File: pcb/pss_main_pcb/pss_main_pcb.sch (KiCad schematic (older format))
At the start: 3 parts

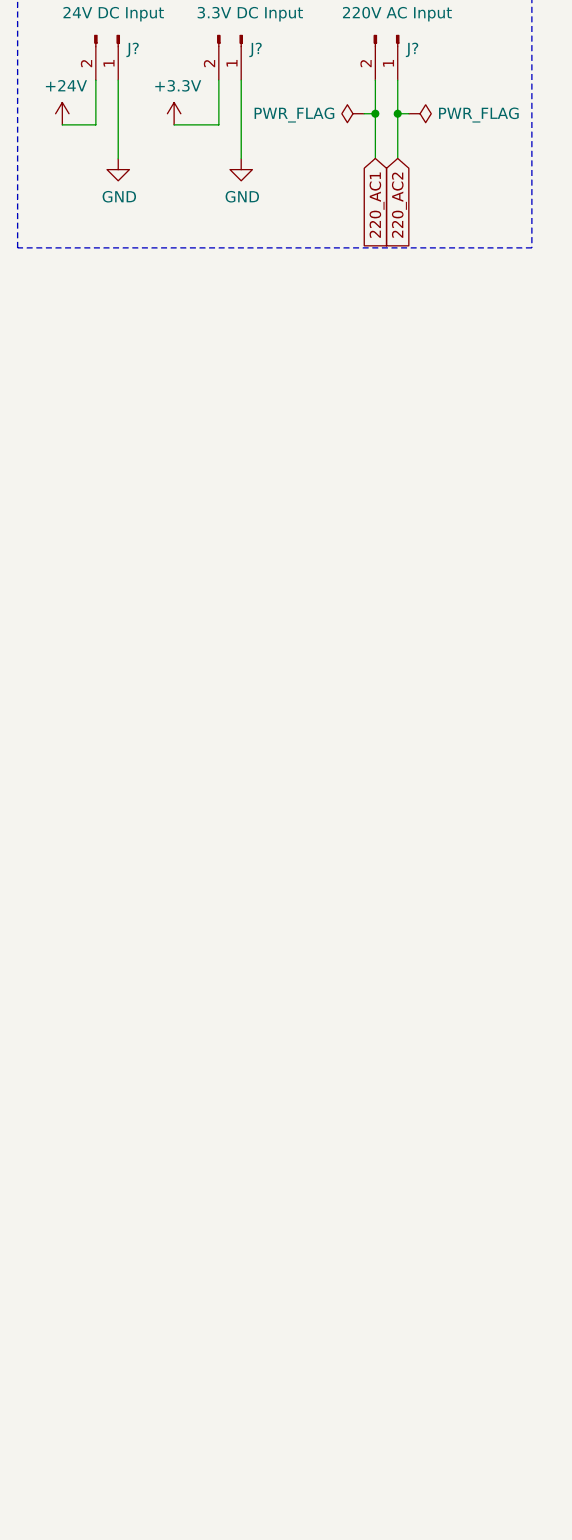
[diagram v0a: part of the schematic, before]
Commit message: Add connectors to schematics
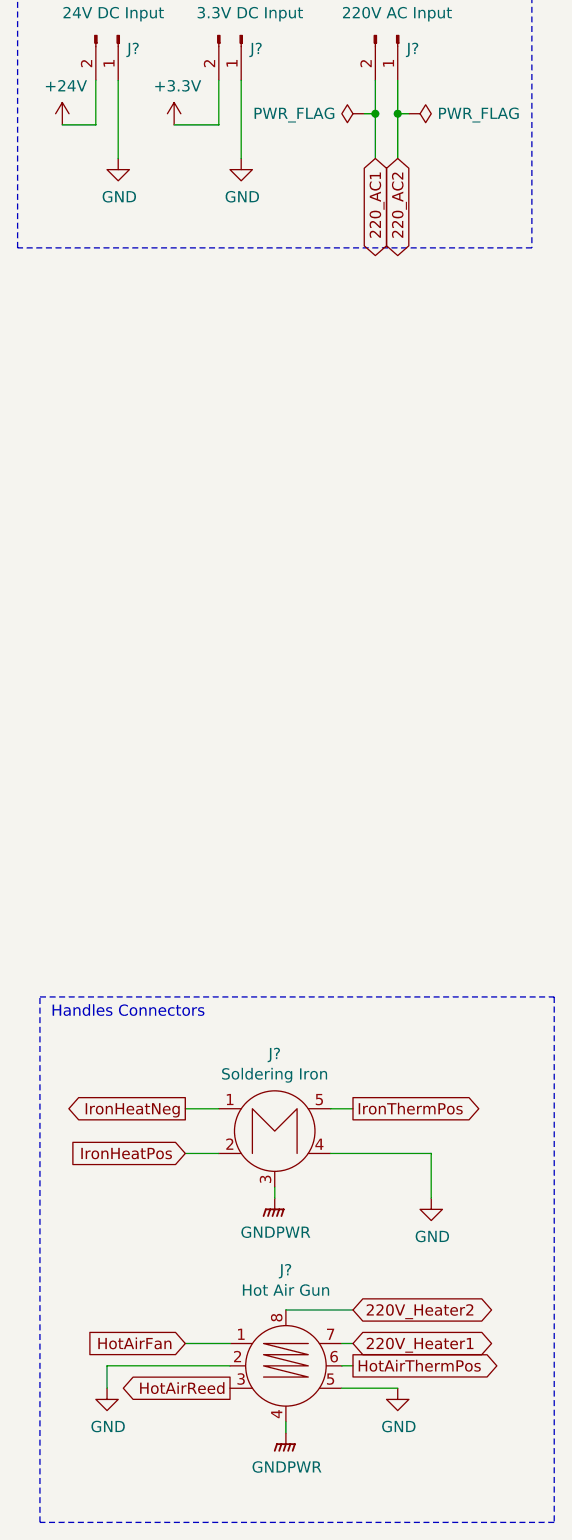
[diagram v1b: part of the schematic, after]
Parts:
- added J?: Soldering Iron, symbol gx16_conn:GX16-M5_connector
- added J?: Hot Air Gun, symbol gx16_conn:GX16-M8_connector
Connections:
- net GND: now also J?.2, J?.4, J?.5
- new net 220V_Heater1: J?.7
- new net 220V_Heater2: J?.8
- new net GNDPWR: J?.3, J?.4
- new net HotAirFan: J?.1
- new net HotAirReed: J?.3
- new net HotAirThermPos: J?.6
- new net IronHeatNeg: J?.1
- new net IronHeatPos: J?.2
- new net IronThermPos: J?.5
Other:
- note added: "Handles Connectors\n"
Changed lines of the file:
@@
 Wire Wire Line
 	2300 1350 2350 1350
-Text GLabel 2200 1550 3    50   Input ~ 0
+Text GLabel 2200 1550 3    50   BiDi ~ 0
 220_AC1
 Wire Wire Line
 	2200 1550 2200 1350
 Connection ~ 2200 1350
-Text GLabel 2300 1550 3    50   Input ~ 0
+Text GLabel 2300 1550 3    50   BiDi ~ 0
 220_AC2
 Wire Wire Line
@@
 Text Notes 650  800  0    50   ~ 0
 Voltage Inputs
+$Comp
+L gx16_conn:GX16-M5_connector J?
+U 1 1 5E88901D
+P 1750 5900
+F 0 "J?" H 1750 6245 50  0000 C CNN
+F 1 "Soldering Iron" H 1750 6154 50  0000 C CNN
+F 2 "" H 2400 5950 50  0001 C CNN
+F 3 "" H 2400 5950 50  0001 C CNN
+	1    1750 5900
+	1    0    0    -1
+$EndComp
+$Comp
+L gx16_conn:GX16-M8_connector J?
+U 1 1 5E88925E
+P 1800 6950
+F 0 "J?" H 1800 7378 50  0000 C CNN
+F 1 "Hot Air Gun" H 1800 7287 50  0000 C CNN
+F 2 "" H 1800 6950 50  0001 C CNN
+F 3 "" H 1800 6950 50  0001 C CNN
+	1    1800 6950
+	1    0    0    -1
+$EndComp
+$Comp
+L power:GNDPWR #PWR?
+U 1 1 5E8894D1
+P 1750 6200
+F 0 "#PWR?" H 1750 6000 50  0001 C CNN
+F 1 "GNDPWR" H 1754 6046 50  0000 C CNN
+F 2 "" H 1750 6150 50  0001 C CNN
+F 3 "" H 1750 6150 50  0001 C CNN
+	1    1750 6200
+	1    0    0    -1
+$EndComp
+Wire Wire Line
+	1750 6150 1750 6200
+$Comp
+L power:GNDPWR #PWR?
+U 1 1 5E889BEB
+P 1800 7250
+F 0 "#PWR?" H 1800 7050 50  0001 C CNN
+F 1 "GNDPWR" H 1804 7096 50  0000 C CNN
+F 2 "" H 1800 7200 50  0001 C CNN
+F 3 "" H 1800 7200 50  0001 C CNN
+	1    1800 7250
+	1    0    0    -1
+$EndComp
+Wire Wire Line
+	1800 7250 1800 7200
+Text GLabel 1350 6000 0    50   Input ~ 0
+IronHeatPos
+Wire Wire Line
+	1350 5800 1500 5800
+Text GLabel 1350 5800 0    50   Output ~ 0
+IronHeatNeg
+Wire Wire Line
+	1350 6000 1500 6000
+Text GLabel 2100 5800 2    50   Output ~ 0
+IronThermPos
+Wire Wire Line
+	2100 5800 2000 5800
+$Comp
+L power:GND #PWR?
+U 1 1 5E88AC54
+P 1000 7050
+F 0 "#PWR?" H 1000 6800 50  0001 C CNN
+F 1 "GND" H 1005 6877 50  0000 C CNN
+F 2 "" H 1000 7050 50  0001 C CNN
+F 3 "" H 1000 7050 50  0001 C CNN
+	1    1000 7050
+	1    0    0    -1
+$EndComp
+Wire Wire Line
+	1000 7050 1000 6950
+Wire Wire Line
+	1000 6950 1550 6950
+Text GLabel 1350 6850 0    50   Input ~ 0
+HotAirFan
+Wire Wire Line
+	1350 6850 1550 6850
+Text GLabel 1550 7050 0    50   Output ~ 0
+HotAirReed
+$Comp
+L power:GND #PWR?
+U 1 1 5E88B481
+P 2300 7050
+F 0 "#PWR?" H 2300 6800 50  0001 C CNN
+F 1 "GND" H 2305 6877 50  0000 C CNN
+F 2 "" H 2300 7050 50  0001 C CNN
+F 3 "" H 2300 7050 50  0001 C CNN
+	1    2300 7050
+	1    0    0    -1
+$EndComp
+Wire Wire Line
+	2050 7050 2300 7050
+$Comp
+L power:GND #PWR?
+U 1 1 5E88B6F3
+P 2450 6200
+F 0 "#PWR?" H 2450 5950 50  0001 C CNN
+F 1 "GND" H 2455 6027 50  0000 C CNN
+F 2 "" H 2450 6200 50  0001 C CNN
+F 3 "" H 2450 6200 50  0001 C CNN
+	1    2450 6200
+	1    0    0    -1
+$EndComp
+Wire Wire Line
+	2450 6200 2450 6000
+Wire Wire Line
+	2000 6000 2450 6000
+Text GLabel 2100 6950 2    50   Output ~ 0
+HotAirThermPos
+Wire Wire Line
+	2050 6950 2100 6950
+Text GLabel 2100 6850 2    50   BiDi ~ 0
+220V_Heater1
+Wire Wire Line
+	2050 6850 2100 6850
+Text GLabel 2100 6700 2    50   BiDi ~ 0
+220V_Heater2
+Wire Notes Line
+	700  5300 3000 5300
+Wire Notes Line
+	3000 5300 3000 7650
+Wire Notes Line
+	3000 7650 700  7650
+Wire Notes Line
+	700  7650 700  5300
+Text Notes 750  5400 0    50   ~ 0
+Handles Connectors\n
+Wire Wire Line
+	2100 6700 1800 6700
 $EndSCHEMATC

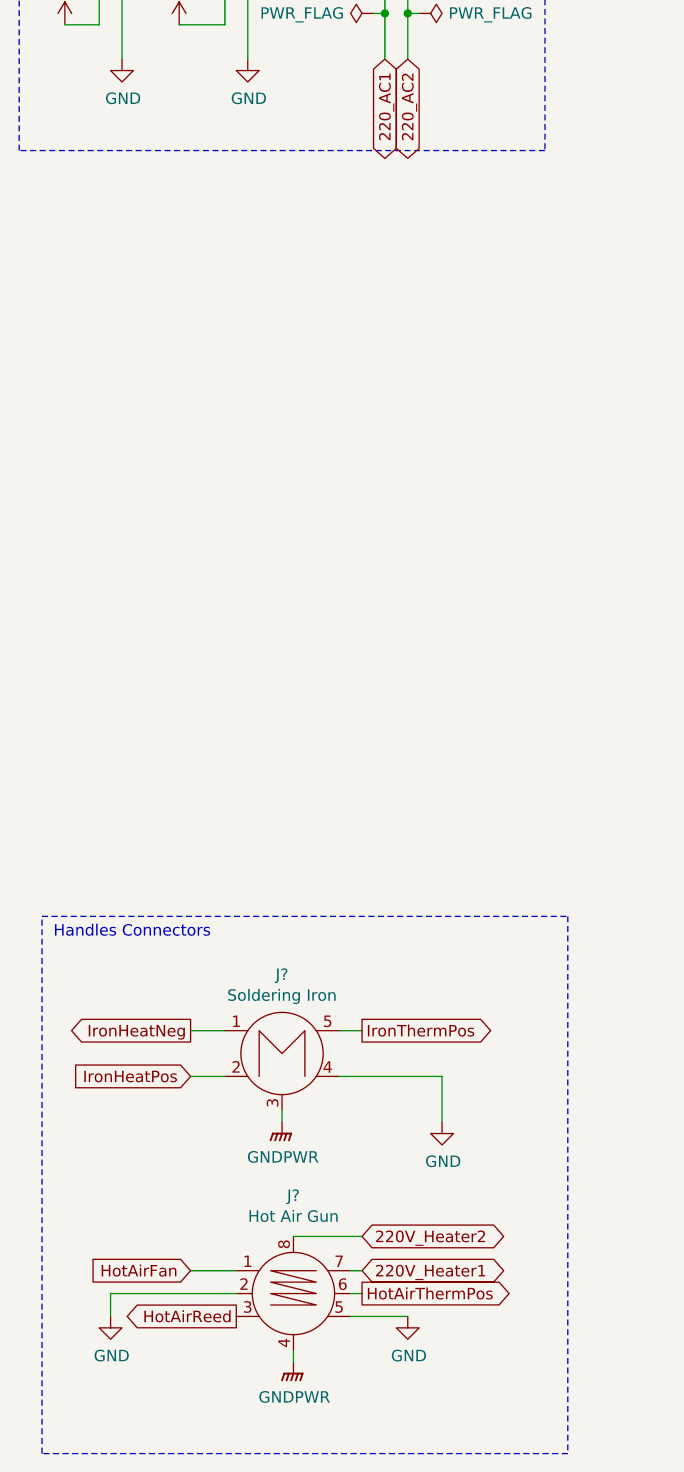
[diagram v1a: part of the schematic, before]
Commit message: Add rotary encoders to schematics
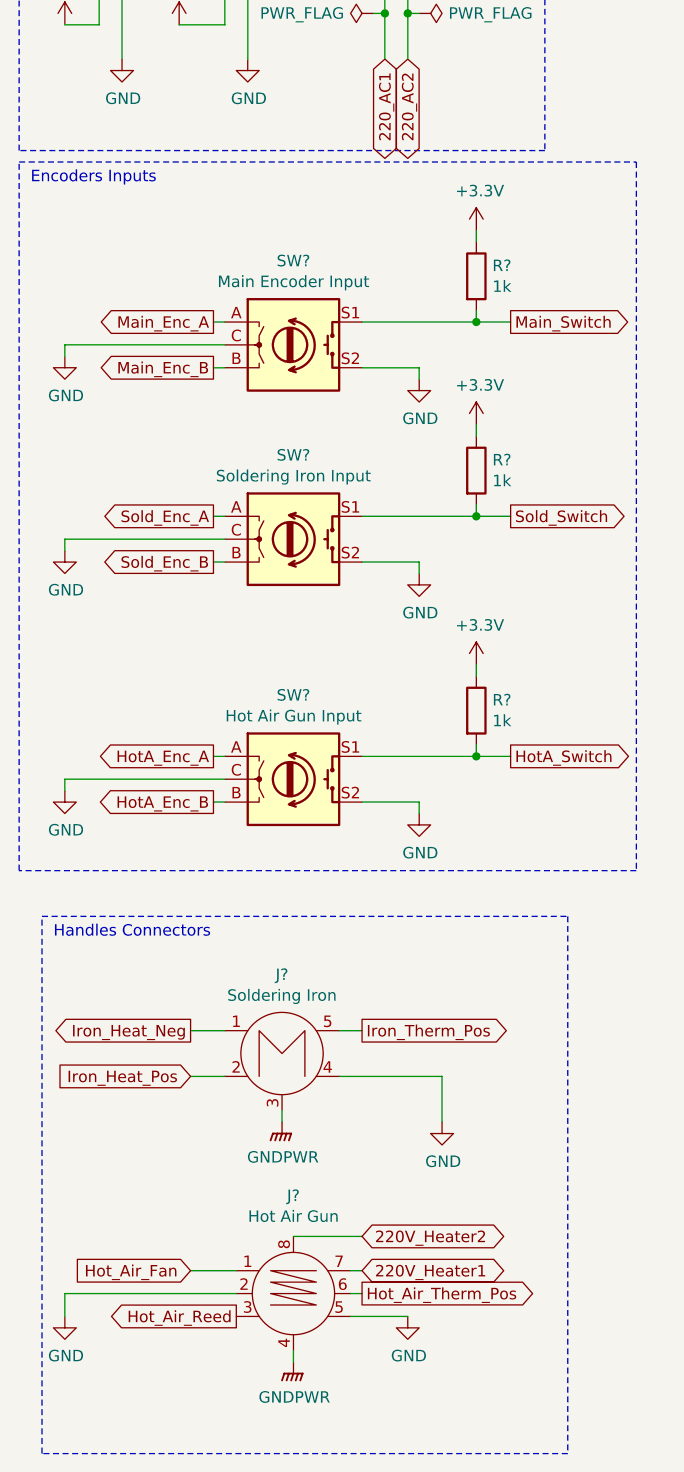
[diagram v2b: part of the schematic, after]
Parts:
- added R? (x3): 1k, symbol Device:R
- added SW?: Main Encoder Input, symbol Device:Rotary_Encoder_Switch
- added SW?: Soldering Iron Input, symbol Device:Rotary_Encoder_Switch
- added SW?: Hot Air Gun Input, symbol Device:Rotary_Encoder_Switch
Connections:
- net +3V3: now also R?.1, R?.1, R?.1
- net GND: now also SW?.C, SW?.C, SW?.C, SW?.S2, SW?.S2, SW?.S2
- net HotAirFan renamed Hot_Air_Fan
- net HotAirReed renamed Hot_Air_Reed
- net HotAirThermPos renamed Hot_Air_Therm_Pos
- net IronHeatNeg renamed Iron_Heat_Neg
- net IronHeatPos renamed Iron_Heat_Pos
- net IronThermPos renamed Iron_Therm_Pos
- new net HotA_Enc_A: SW?.A
- new net HotA_Enc_B: SW?.B
- new net HotA_Switch: R?.2, SW?.S1
- new net Main_Enc_A: SW?.A
- new net Main_Enc_B: SW?.B
- new net Main_Switch: R?.2, SW?.S1
- new net Sold_Enc_A: SW?.A
- new net Sold_Enc_B: SW?.B
- new net Sold_Switch: R?.2, SW?.S1
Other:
- note added: "Encoders Inputs"

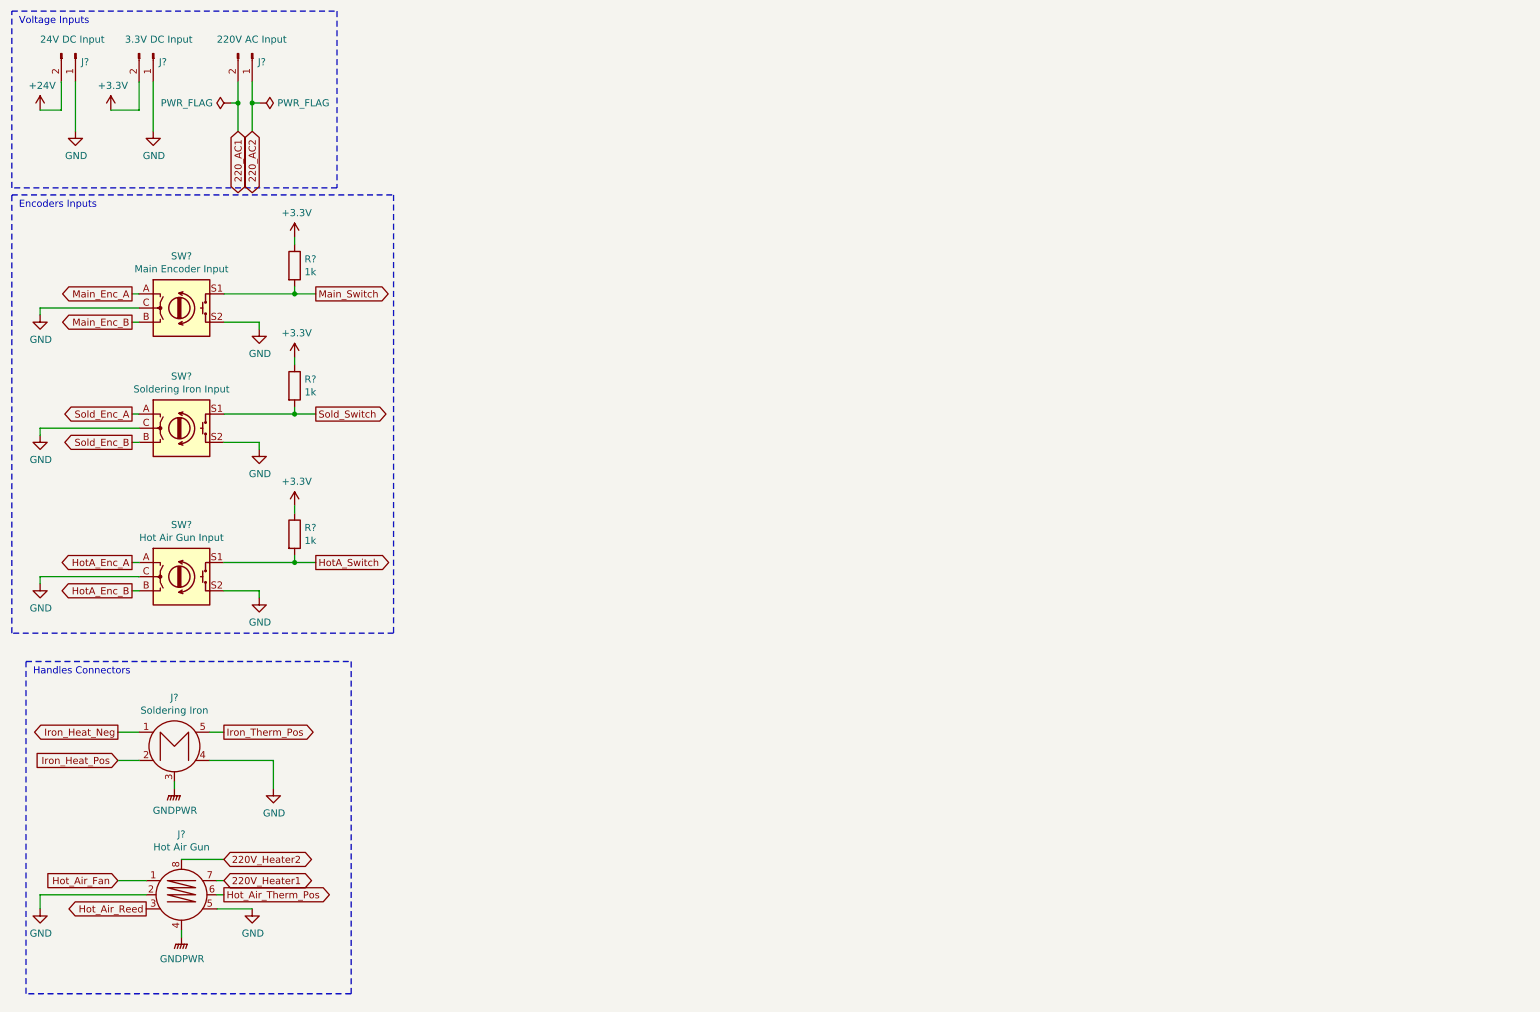
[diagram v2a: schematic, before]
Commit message: Add voltage converters and soldering heater
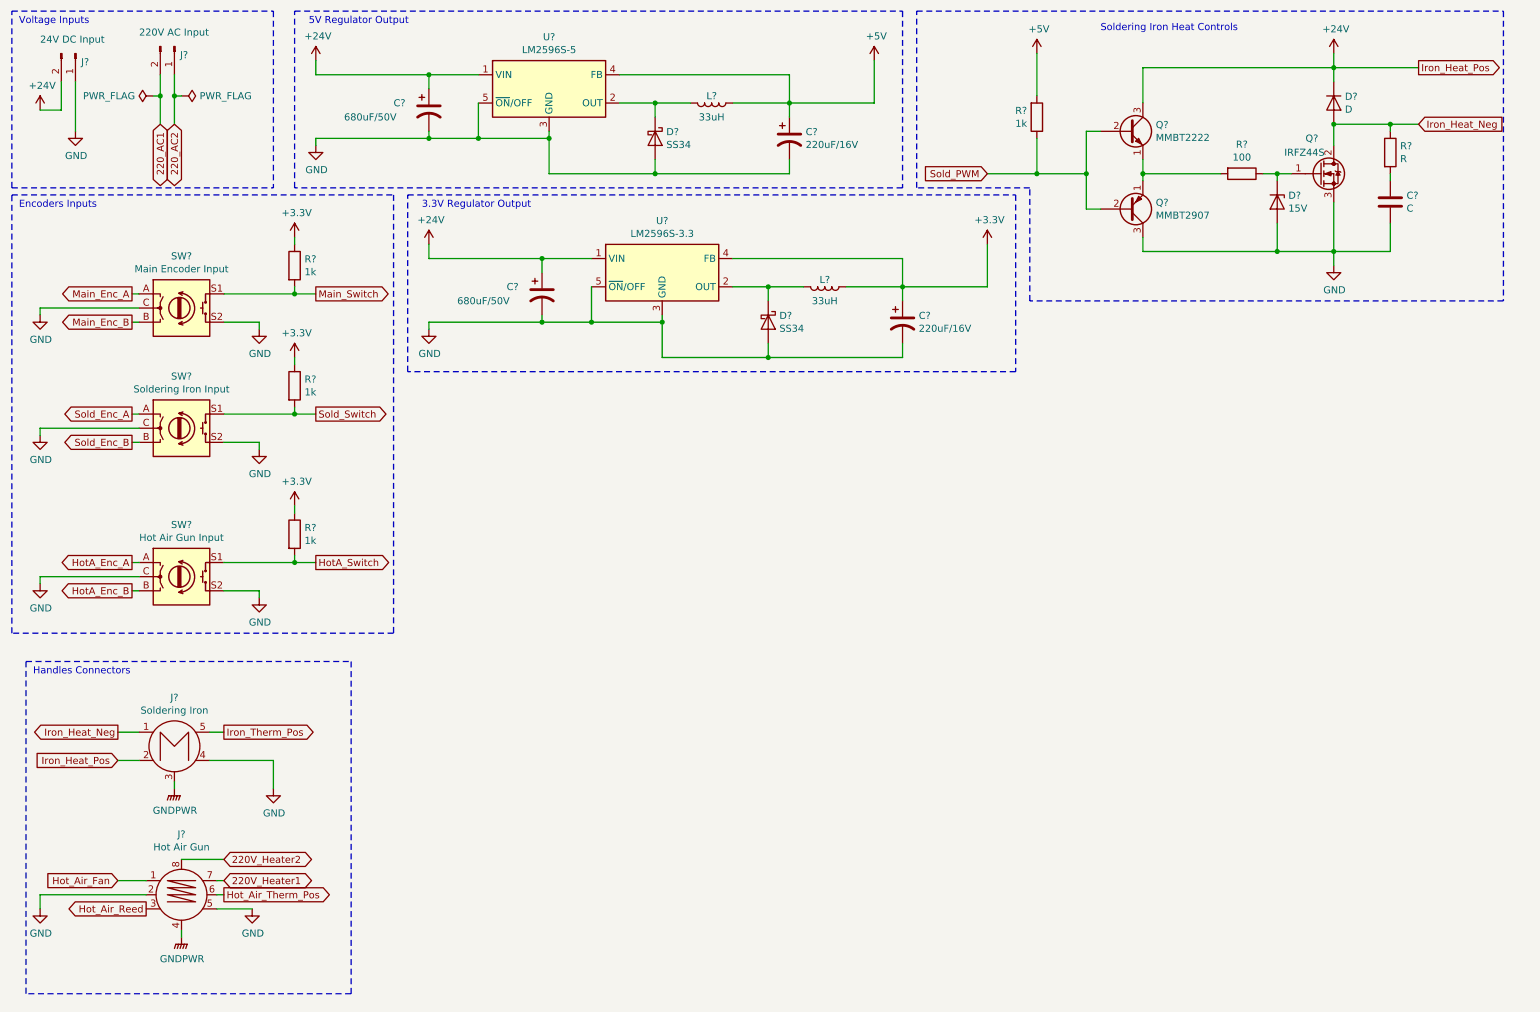
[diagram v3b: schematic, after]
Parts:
- removed J?: 3.3V DC Input, symbol Connector:Conn_01x02_Male
- added C?: C, symbol Device:C
- added C? (x2): 680uF/50V, symbol Device:CP1
- added C? (x2): 220uF/16V, symbol Device:CP1
- added D?: D, symbol Device:D
- added D?: 15V, symbol Device:D_Zener
- added D? (x2): SS34, symbol Device:D_Schottky
- added L? (x2): 33uH, symbol Device:L
- added Q?: IRFZ44S, Package_TO_SOT_THT:TO-220-3_Vertical, symbol Transistors_custom:IRFZ44S
- added Q?: MMBT2222, Package_TO_SOT_THT:TO-92_Inline, symbol Transistors_custom:MMBT2222
- added Q?: MMBT2907, Package_TO_SOT_THT:TO-92_Inline, symbol Transistors_custom:MMBT2907
- added R?: 100, symbol Device:R
- added R?: 1k, symbol Device:R
- added R?: R, symbol Device:R
- added U?: LM2596S-5, Package_TO_SOT_SMD:TO-263-5_TabPin3, symbol Regulator_Switching:LM2596S-5
- added U?: LM2596S-3.3, Package_TO_SOT_SMD:TO-263-5_TabPin3, symbol Regulator_Switching:LM2596S-3.3
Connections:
- net Iron_Heat_Pos is gone; now on net +24V: J?.2
- net +24V: now also C?.1, C?.1, D?.1 (K), Q?.3 (C), U?.1 (VIN), U?.1 (VIN)
- net +3V3: now also C?.1, L?.1, U?.4 (FB)
- net GND: now also C?.2, C?.2, C?.2, C?.2, C?.2, D?.2 (A), D?.2 (A), D?.2 (A), Q?.3 (C), Q?.3 (S), U?.3 (GND), U?.3 (GND), U?.5 (~ON~/OFF), U?.5 (~ON~/OFF)
- net Iron_Heat_Neg: now also D?.2 (A), Q?.2 (D), R?.1
- new net: D?.1 (K), Q?.1 (G), R?.1
- new net: Q?.1 (E), Q?.1 (E), R?.2
- new net: C?.1, R?.2
- new net: D?.1 (K), L?.2, U?.2 (OUT) (x2)
- new net +5V: C?.1, L?.1, R?.2, U?.4 (FB)
- new net Sold_PWM: Q?.2 (B), Q?.2 (B), R?.1
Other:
- note added: "3.3V Regulator Output"
- note added: "5V Regulator Output"
- note added: "Soldering Iron Heat Controls\n"
- moved on the sheet: J?
